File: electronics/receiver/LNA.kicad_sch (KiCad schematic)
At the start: 25 parts, among them J407 Conn_Coaxial, U407 AS179-92LF, U408 PSA4-5043, U409 AS179-92LF

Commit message: Update values
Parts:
- R412, R414, R415, R417: value R -> 100R
- R413, R416: value R -> 68R
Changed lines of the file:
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@@
+    (effects (font (size 1.27 1.27)) (justify left bottom))
+  )
+  (label "9.6 dB attenuator" (at 173.99 68.58 0)
+    (effects (font (size 1.27 1.27)) (justify left bottom))
+  )
+  (label "9.6 dB attenuator" (at 119.38 104.14 0)
+    (effects (font (size 1.27 1.27)) (justify left bottom))
+  )
+  (label "Gain 13dB, or -10dB" (at 140.97 38.1 0)
     (effects (font (size 1.27 1.27)) (justify left bottom))
   )
@@
   (symbol (lib_id "Device:R") (at 113.03 106.68 90) (unit 1)
     (in_bom yes) (on_board yes) (fields_autoplaced)
-    (property "Reference" "R413" (id 0) (at 113.03 101.6975 90))
-    (property "Value" "R" (id 1) (at 113.03 104.4726 90))
+    (property "Reference" "R413" (id 0) (at 113.03 100.33 90))
+    (property "Value" "68R" (id 1) (at 113.03 102.87 90))
     (property "Footprint" "Resistor_SMD:R_0805_2012Metric_Pad1.20x1.40mm_HandSolder" (id 2) (at 113.03 108.458 90)
       (effects (font (size 1.27 1.27)) hide)
@@
   (symbol (lib_id "Device:R") (at 190.5 82.55 0) (unit 1)
     (in_bom yes) (on_board yes) (fields_autoplaced)
-    (property "Reference" "R417" (id 0) (at 192.278 81.6415 0)
-      (effects (font (size 1.27 1.27)) (justify left))
-    )
-    (property "Value" "R" (id 1) (at 192.278 84.4166 0)
+    (property "Reference" "R417" (id 0) (at 193.04 81.2799 0)
+      (effects (font (size 1.27 1.27)) (justify left))
+    )
+    (property "Value" "100R" (id 1) (at 193.04 83.8199 0)
       (effects (font (size 1.27 1.27)) (justify left))
     )
@@
   (symbol (lib_id "Device:R") (at 123.19 111.76 0) (unit 1)
     (in_bom yes) (on_board yes) (fields_autoplaced)
-    (property "Reference" "R414" (id 0) (at 124.968 110.8515 0)
-      (effects (font (size 1.27 1.27)) (justify left))
-    )
-    (property "Value" "R" (id 1) (at 124.968 113.6266 0)
+    (property "Reference" "R414" (id 0) (at 125.73 110.4899 0)
+      (effects (font (size 1.27 1.27)) (justify left))
+    )
+    (property "Value" "100R" (id 1) (at 125.73 113.0299 0)
       (effects (font (size 1.27 1.27)) (justify left))
     )
@@
   (symbol (lib_id "Device:R") (at 180.34 77.47 90) (unit 1)
     (in_bom yes) (on_board yes) (fields_autoplaced)
-    (property "Reference" "R416" (id 0) (at 180.34 72.4875 90))
-    (property "Value" "R" (id 1) (at 180.34 75.2626 90))
+    (property "Reference" "R416" (id 0) (at 180.34 71.12 90))
+    (property "Value" "68R" (id 1) (at 180.34 73.66 90))
     (property "Footprint" "Resistor_SMD:R_0805_2012Metric_Pad1.20x1.40mm_HandSolder" (id 2) (at 180.34 79.248 90)
       (effects (font (size 1.27 1.27)) hide)
@@
   (symbol (lib_id "Device:R") (at 168.91 82.55 0) (unit 1)
     (in_bom yes) (on_board yes) (fields_autoplaced)
-    (property "Reference" "R415" (id 0) (at 170.688 81.6415 0)
-      (effects (font (size 1.27 1.27)) (justify left))
-    )
-    (property "Value" "R" (id 1) (at 170.688 84.4166 0)
+    (property "Reference" "R415" (id 0) (at 171.45 81.2799 0)
+      (effects (font (size 1.27 1.27)) (justify left))
+    )
+    (property "Value" "100R" (id 1) (at 171.45 83.8199 0)
       (effects (font (size 1.27 1.27)) (justify left))
     )
@@
   (symbol (lib_id "Device:R") (at 101.6 111.76 0) (unit 1)
     (in_bom yes) (on_board yes) (fields_autoplaced)
-    (property "Reference" "R412" (id 0) (at 103.378 110.8515 0)
-      (effects (font (size 1.27 1.27)) (justify left))
-    )
-    (property "Value" "R" (id 1) (at 103.378 113.6266 0)
-      (effects (font (size 1.27 1.27)) (justify left))
-    )
+    (property "Reference" "R412" (id 0) (at 104.14 110.4899 0)
+      (effects (font (size 1.27 1.27)) (justify left))
+    )
+    (property "Value" "100R" (id 1) (at 104.14 113.0299 0)
+      (effects (font (size 1.27 1.27)) (justify left))
+    )

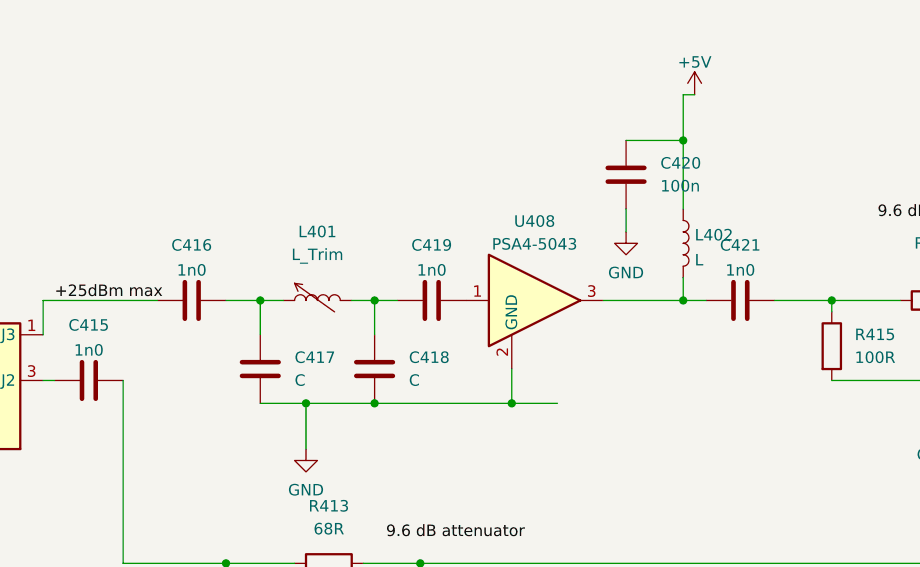
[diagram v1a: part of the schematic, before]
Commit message: Update
Schematic values
Add some Data sheets
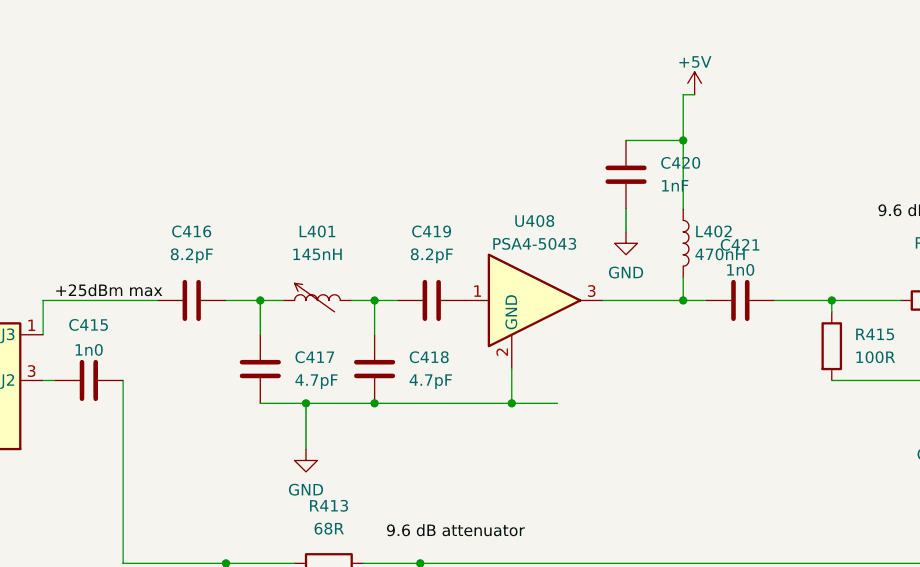
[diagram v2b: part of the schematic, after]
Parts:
- C416, C419: value 1n0 -> 8.2pF
- C417, C418: value C -> 4.7pF
- C420: value 100n -> 1nF
- L401: value L_Trim -> 145nH
- L402: value L -> 470nH
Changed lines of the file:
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@@
     (in_bom yes) (on_board yes) (fields_autoplaced)
     (property "Reference" "L401" (id 0) (at 111.76 69.85 90))
-    (property "Value" "L_Trim" (id 1) (at 111.76 72.39 90))
+    (property "Value" "145nH" (id 1) (at 111.76 72.39 90))
     (property "Footprint" "Inductor_THT:L_Radial_L10.2mm_W10.2mm_Px7.62mm_Py7.62mm_Pulse_LP-30" (id 2) (at 111.76 77.47 0)
       (effects (font (size 1.27 1.27)) hide)
@@
       (effects (font (size 1.27 1.27)) (justify left))
     )
-    (property "Value" "C" (id 1) (at 121.92 86.3599 0)
+    (property "Value" "4.7pF" (id 1) (at 121.92 86.3599 0)
       (effects (font (size 1.27 1.27)) (justify left))
     )
@@
   (symbol (lib_id "Device:C") (at 124.46 77.47 270) (unit 1)
     (in_bom yes) (on_board yes) (fields_autoplaced)
-    (property "Reference" "C419" (id 0) (at 124.46 71.3445 90))
-    (property "Value" "1n0" (id 1) (at 124.46 74.1196 90))
+    (property "Reference" "C419" (id 0) (at 124.46 69.85 90))
+    (property "Value" "8.2pF" (id 1) (at 124.46 72.39 90))
     (property "Footprint" "Capacitor_SMD:C_0805_2012Metric" (id 2) (at 120.65 78.4352 0)
       (effects (font (size 1.27 1.27)) hide)
@@
   (symbol (lib_id "Device:C") (at 97.79 77.47 270) (unit 1)
     (in_bom yes) (on_board yes) (fields_autoplaced)
-    (property "Reference" "C416" (id 0) (at 97.79 71.3445 90))
-    (property "Value" "1n0" (id 1) (at 97.79 74.1196 90))
+    (property "Reference" "C416" (id 0) (at 97.79 69.85 90))
+    (property "Value" "8.2pF" (id 1) (at 97.79 72.39 90))
     (property "Footprint" "Capacitor_SMD:C_0805_2012Metric" (id 2) (at 93.98 78.4352 0)
       (effects (font (size 1.27 1.27)) hide)
@@
   (symbol (lib_id "Device:L") (at 152.4 71.12 0) (unit 1)
     (in_bom yes) (on_board yes) (fields_autoplaced)
-    (property "Reference" "L402" (id 0) (at 153.67 70.2115 0)
-      (effects (font (size 1.27 1.27)) (justify left))
-    )
-    (property "Value" "L" (id 1) (at 153.67 72.9866 0)
+    (property "Reference" "L402" (id 0) (at 153.67 69.8499 0)
+      (effects (font (size 1.27 1.27)) (justify left))
+    )
+    (property "Value" "470nH" (id 1) (at 153.67 72.3899 0)
       (effects (font (size 1.27 1.27)) (justify left))
     )
@@
       (effects (font (size 1.27 1.27)) (justify left))
     )
-    (property "Value" "100n" (id 1) (at 149.86 64.7699 0)
+    (property "Value" "1nF" (id 1) (at 149.86 64.7699 0)
       (effects (font (size 1.27 1.27)) (justify left))
     )
@@
       (effects (font (size 1.27 1.27)) (justify left))
     )
-    (property "Value" "C" (id 1) (at 109.22 86.3599 0)
-      (effects (font (size 1.27 1.27)) (justify left))
-    )
+    (property "Value" "4.7pF" (id 1) (at 109.22 86.3599 0)
+      (effects (font (size 1.27 1.27)) (justify left))
+    )

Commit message: Repair
Fix Github commit problem
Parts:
- C419: renamed from C416; value 8.2pF -> 15pF
- C420: renamed from C417; value 4.7pF -> 10pF
- C421: renamed from C418; value 4.7pF -> 10pF
- C422: renamed from C419; value 8.2pF -> 15pF
- L401: value 145nH -> 105nH
- renumbered C413 to C416, C414 to C417, C415 to C418, C420 to C423, C421 to C424, C422 to C425, C423 to C426, C424 to C427
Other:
- note added: "+19dBm (1dB compression)"
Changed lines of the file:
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@@
     (stroke (width 0) (type default) (color 0 0 0 0))
+  )
+  (text "+19dBm (1dB compression)\n" (at 137.16 46.99 0)
+    (effects (font (size 1.27 1.27)) (justify left bottom))
   )
   (label "PIN Limiter" (at 38.1 83.82 0)
@@
     (in_bom yes) (on_board yes) (fields_autoplaced)
     (property "Reference" "L401" (id 0) (at 111.76 69.85 90))
-    (property "Value" "145nH" (id 1) (at 111.76 72.39 90))
+    (property "Value" "105nH" (id 1) (at 111.76 72.39 90))
     (property "Footprint" "Inductor_THT:L_Radial_L10.2mm_W10.2mm_Px7.62mm_Py7.62mm_Pulse_LP-30" (id 2) (at 111.76 77.47 0)
       (effects (font (size 1.27 1.27)) hide)
@@
   (symbol (lib_id "Device:C") (at 250.19 80.01 90) (unit 1)
     (in_bom yes) (on_board yes) (fields_autoplaced)
-    (property "Reference" "C424" (id 0) (at 249.3553 77.089 0)
+    (property "Reference" "C427" (id 0) (at 249.3553 77.089 0)
       (effects (font (size 1.27 1.27)) (justify left))
     )
@@
   (symbol (lib_id "Device:C") (at 118.11 85.09 0) (unit 1)
     (in_bom yes) (on_board yes) (fields_autoplaced)
-    (property "Reference" "C418" (id 0) (at 121.92 83.8199 0)
-      (effects (font (size 1.27 1.27)) (justify left))
-    )
-    (property "Value" "4.7pF" (id 1) (at 121.92 86.3599 0)
+    (property "Reference" "C421" (id 0) (at 121.92 83.8199 0)
+      (effects (font (size 1.27 1.27)) (justify left))
+    )
+    (property "Value" "10pF" (id 1) (at 121.92 86.3599 0)
       (effects (font (size 1.27 1.27)) (justify left))
     )
@@
   (symbol (lib_id "Device:C") (at 54.61 83.82 90) (unit 1)
     (in_bom yes) (on_board yes) (fields_autoplaced)
-    (property "Reference" "C414" (id 0) (at 54.61 77.9612 90))
+    (property "Reference" "C417" (id 0) (at 54.61 77.9612 90))
     (property "Value" "1n0" (id 1) (at 54.61 80.4981 90))
     (property "Footprint" "Capacitor_SMD:C_0805_2012Metric_Pad1.18x1.45mm_HandSolder" (id 2) (at 58.42 82.8548 0)
@@
   (symbol (lib_id "Device:C") (at 124.46 77.47 270) (unit 1)
     (in_bom yes) (on_board yes) (fields_autoplaced)
-    (property "Reference" "C419" (id 0) (at 124.46 69.85 90))
-    (property "Value" "8.2pF" (id 1) (at 124.46 72.39 90))
+    (property "Reference" "C422" (id 0) (at 124.46 69.85 90))
+    (property "Value" "15pF" (id 1) (at 124.46 72.39 90))
     (property "Footprint" "Capacitor_SMD:C_0805_2012Metric" (id 2) (at 120.65 78.4352 0)
       (effects (font (size 1.27 1.27)) hide)
@@
   (symbol (lib_id "Device:C") (at 97.79 77.47 270) (unit 1)
     (in_bom yes) (on_board yes) (fields_autoplaced)
-    (property "Reference" "C416" (id 0) (at 97.79 69.85 90))
-    (property "Value" "8.2pF" (id 1) (at 97.79 72.39 90))
+    (property "Reference" "C419" (id 0) (at 97.79 69.85 90))
+    (property "Value" "15pF" (id 1) (at 97.79 72.39 90))
     (property "Footprint" "Capacitor_SMD:C_0805_2012Metric" (id 2) (at 93.98 78.4352 0)
       (effects (font (size 1.27 1.27)) hide)
@@
   (symbol (lib_id "Device:C") (at 86.36 86.36 90) (mirror x) (unit 1)
     (in_bom yes) (on_board yes) (fields_autoplaced)
-    (property "Reference" "C415" (id 0) (at 86.36 80.2345 90))
+    (property "Reference" "C418" (id 0) (at 86.36 80.2345 90))
     (property "Value" "1n0" (id 1) (at 86.36 83.0096 90))
     (property "Footprint" "Capacitor_SMD:C_0805_2012Metric" (id 2) (at 90.17 87.3252 0)
@@
   (symbol (lib_id "Device:C") (at 33.02 83.82 90) (unit 1)
     (in_bom yes) (on_board yes) (fields_autoplaced)
-    (property "Reference" "C413" (id 0) (at 33.02 77.6945 90))
+    (property "Reference" "C416" (id 0) (at 33.02 77.6945 90))
     (property "Value" "1n0" (id 1) (at 33.02 80.4696 90))
     (property "Footprint" "Capacitor_SMD:C_0805_2012Metric_Pad1.18x1.45mm_HandSolder" (id 2) (at 36.83 82.8548 0)
@@
   (symbol (lib_id "Device:C") (at 208.28 77.47 270) (unit 1)
     (in_bom yes) (on_board yes) (fields_autoplaced)
-    (property "Reference" "C422" (id 0) (at 209.1147 80.391 0)
+    (property "Reference" "C425" (id 0) (at 209.1147 80.391 0)
       (effects (font (size 1.27 1.27)) (justify left))
     )
@@
   (symbol (lib_id "Device:C") (at 146.05 63.5 0) (unit 1)
     (in_bom yes) (on_board yes) (fields_autoplaced)
-    (property "Reference" "C420" (id 0) (at 149.86 62.2299 0)
+    (property "Reference" "C423" (id 0) (at 149.86 62.2299 0)
       (effects (font (size 1.27 1.27)) (justify left))
     )
@@
   (symbol (lib_id "Device:C") (at 209.55 97.79 0) (unit 1)
     (in_bom yes) (on_board yes) (fields_autoplaced)
-    (property "Reference" "C423" (id 0) (at 212.471 96.9553 0)
+    (property "Reference" "C426" (id 0) (at 212.471 96.9553 0)
       (effects (font (size 1.27 1.27)) (justify left))
     )
@@
   (symbol (lib_id "Device:C") (at 105.41 85.09 0) (unit 1)
     (in_bom yes) (on_board yes) (fields_autoplaced)
-    (property "Reference" "C417" (id 0) (at 109.22 83.8199 0)
-      (effects (font (size 1.27 1.27)) (justify left))
-    )
-    (property "Value" "4.7pF" (id 1) (at 109.22 86.3599 0)
+    (property "Reference" "C420" (id 0) (at 109.22 83.8199 0)
+      (effects (font (size 1.27 1.27)) (justify left))
+    )
+    (property "Value" "10pF" (id 1) (at 109.22 86.3599 0)
       (effects (font (size 1.27 1.27)) (justify left))
     )
@@
   (symbol (lib_id "Device:C") (at 158.75 77.47 90) (unit 1)
     (in_bom yes) (on_board yes) (fields_autoplaced)
-    (property "Reference" "C421" (id 0) (at 158.75 71.3445 90))
+    (property "Reference" "C424" (id 0) (at 158.75 71.3445 90))
     (property "Value" "1n0" (id 1) (at 158.75 74.1196 90))
     (property "Footprint" "Capacitor_SMD:C_0805_2012Metric" (id 2) (at 162.56 76.5048 0)
